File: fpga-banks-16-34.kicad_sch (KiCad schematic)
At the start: 24 parts, among them U3002 XC7K160T-FFG676, U9001 Oscillator_SMD_100MHz_ASFLMB, U9002 PCA9517A_TSSOP

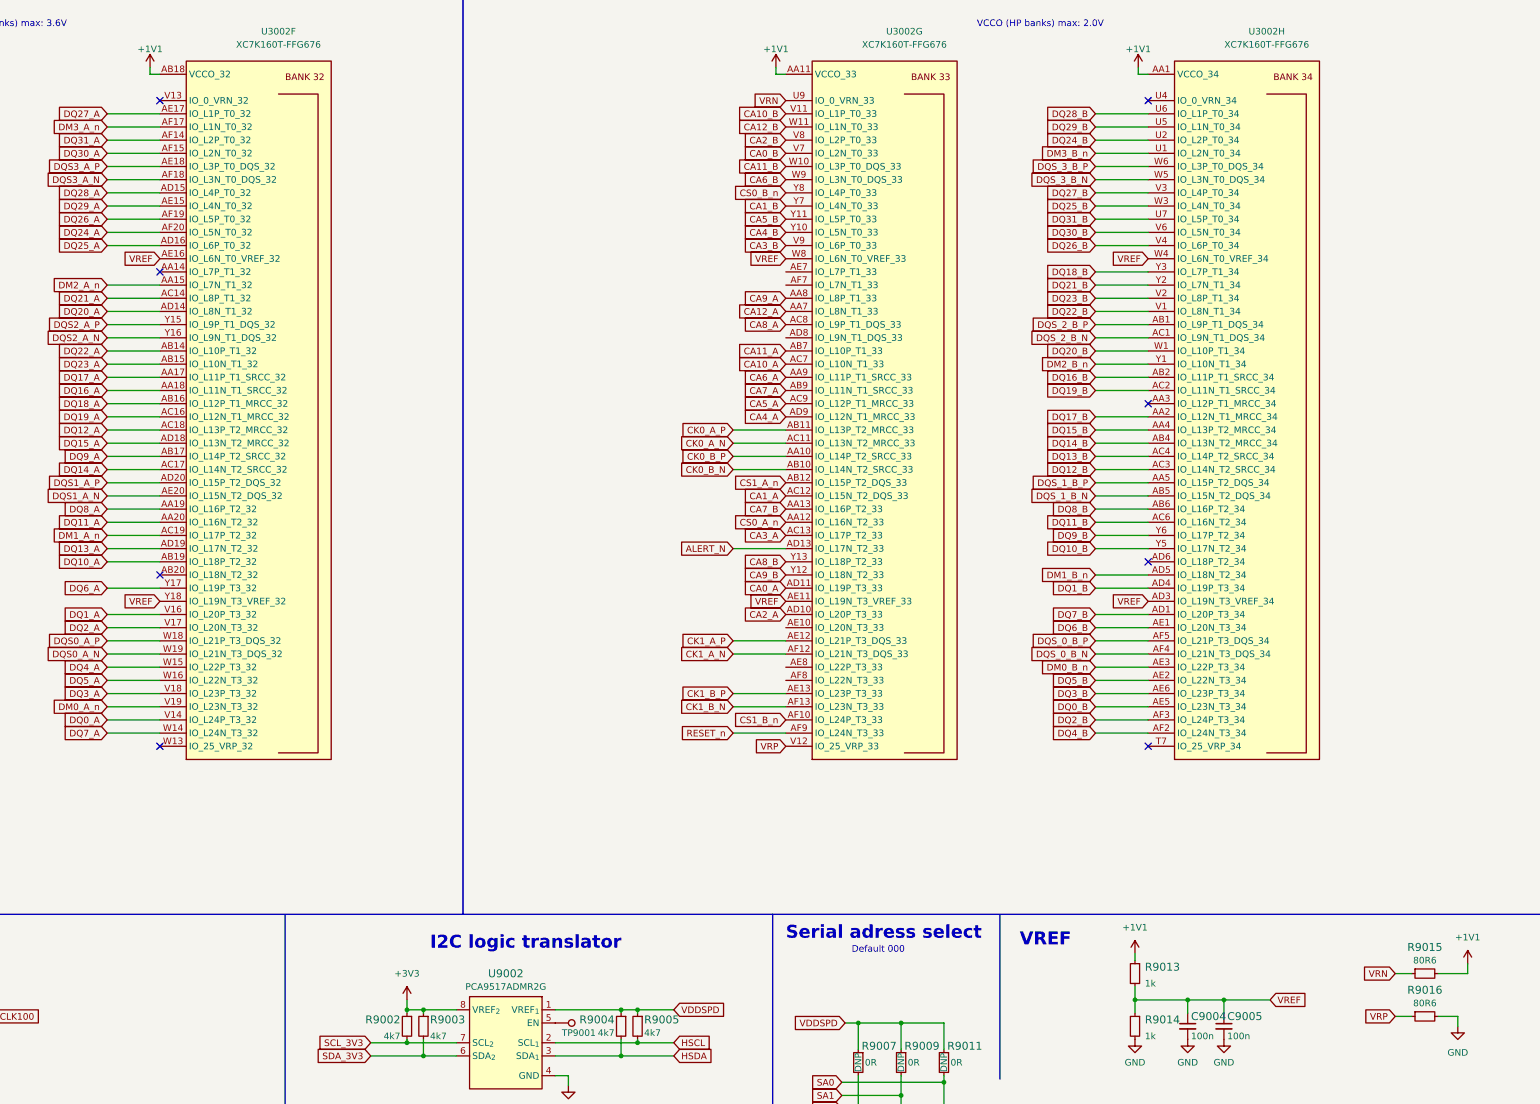
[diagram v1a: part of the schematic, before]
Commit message: Improve DDR assigment, connect ECC to remaining pins, cleanup not used components, continue placement of misc. components
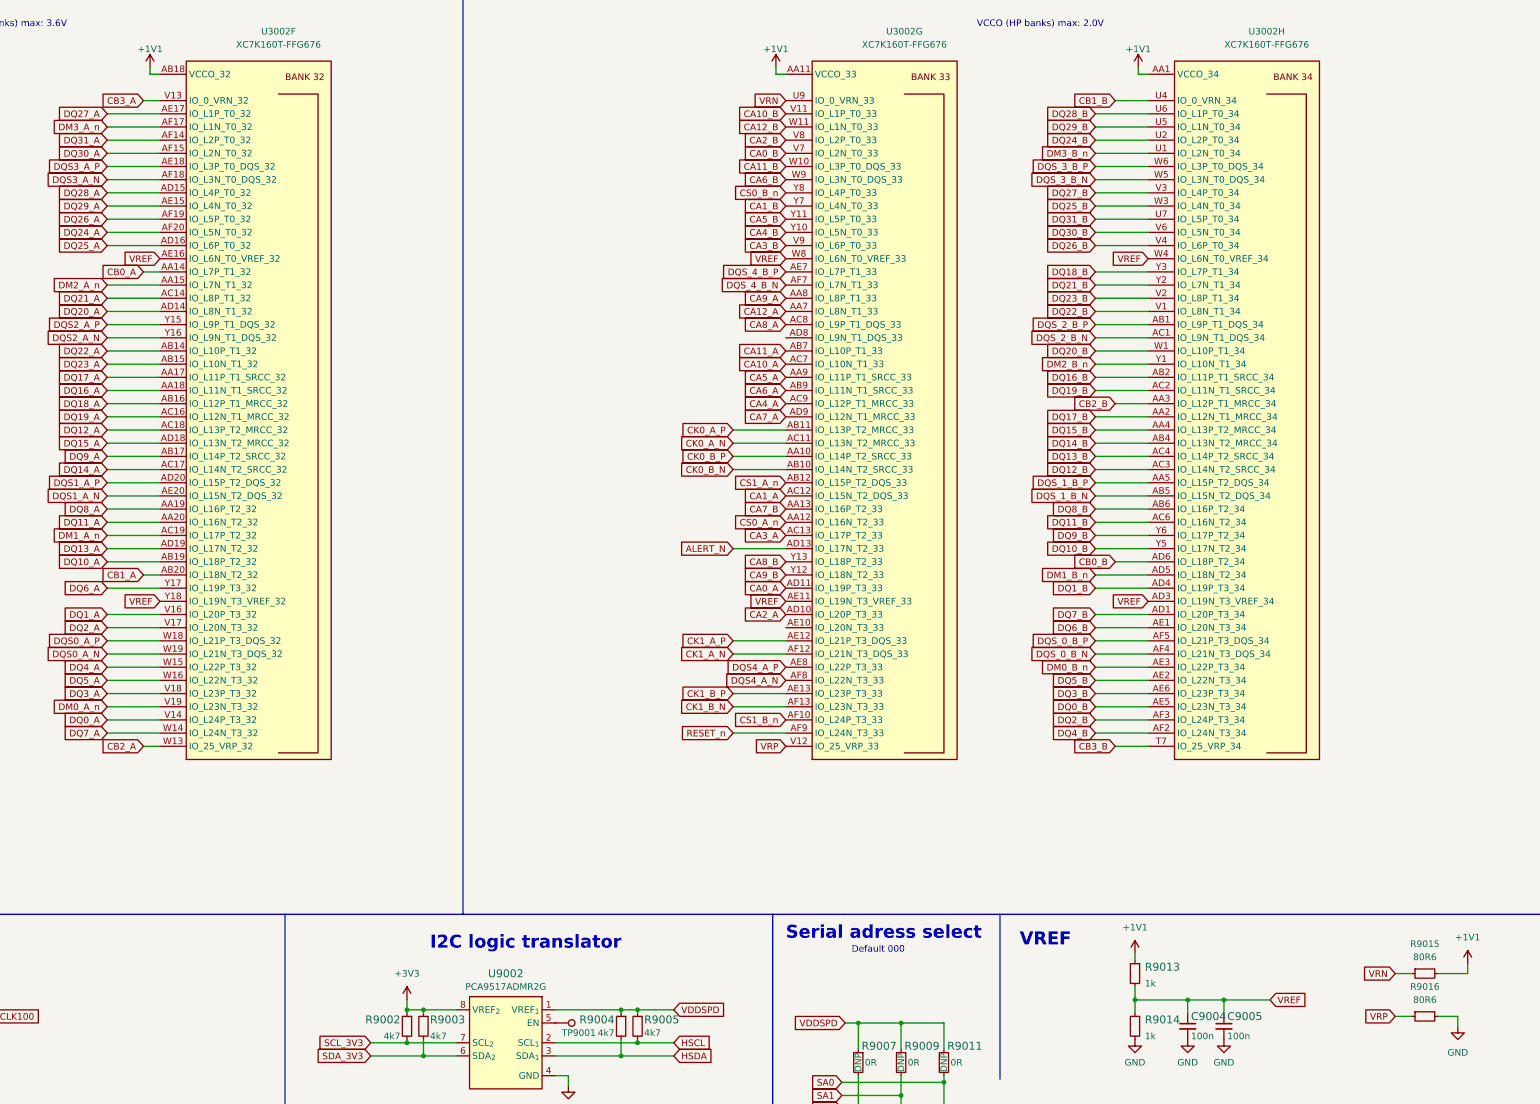
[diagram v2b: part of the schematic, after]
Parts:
- removed R9015, R9016: R_80R6_0603, data-center-rdimm-ddr4-tester-footprints:R_0603_1608Metric, symbol data-center-rdimm-ddr4-tester:R_80R6_0603
- added R9015, R9016: R_80R6_0402_EIA, antmicro-footprints:R_0402_1005Metric_EIA, symbol Resistors0402:R_80R6_0402_EIA
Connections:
- net +1V1: now also R9015.2
- net CA4_A: now also U3002.AC9 (IO_L12P_T1_MRCC_33); no longer U3002.AD9 (IO_L12N_T1_MRCC_33)
- net CA5_A: now also U3002.AA9 (IO_L11P_T1_SRCC_33); no longer U3002.AC9 (IO_L12P_T1_MRCC_33)
- net CA6_A: now also U3002.AB9 (IO_L11N_T1_SRCC_33); no longer U3002.AA9 (IO_L11P_T1_SRCC_33)
- net CA7_A: now also U3002.AD9 (IO_L12N_T1_MRCC_33); no longer U3002.AB9 (IO_L11N_T1_SRCC_33)
- net GND: now also R9016.2
- net VRN: now also R9015.1
- net VRP: now also R9016.1
- net CB0_A: now reaches U3002.AA14 (IO_L7P_T1_32)
- net CB1_A: now reaches U3002.AB20 (IO_L18N_T2_32)
- net CB3_A: now reaches U3002.V13 (IO_0_VRN_32)
- net CB2_A: now reaches U3002.W13 (IO_25_VRP_32)
- net DQS_4_B_P: now reaches U3002.AE7 (IO_L7P_T1_33)
- net DQS4_A_P: now reaches U3002.AE8 (IO_L22P_T3_33)
- net DQS_4_B_N: now reaches U3002.AF7 (IO_L7N_T1_33)
- net DQS4_A_N: now reaches U3002.AF8 (IO_L22N_T3_33)
- net CB2_B: now reaches U3002.AA3 (IO_L12P_T1_MRCC_34)
- net CB0_B: now reaches U3002.AD6 (IO_L18P_T2_34)
- net CB3_B: now reaches U3002.T7 (IO_25_VRP_34)
- net CB1_B: now reaches U3002.U4 (IO_0_VRN_34)
- no-connect marks 41 -> 33

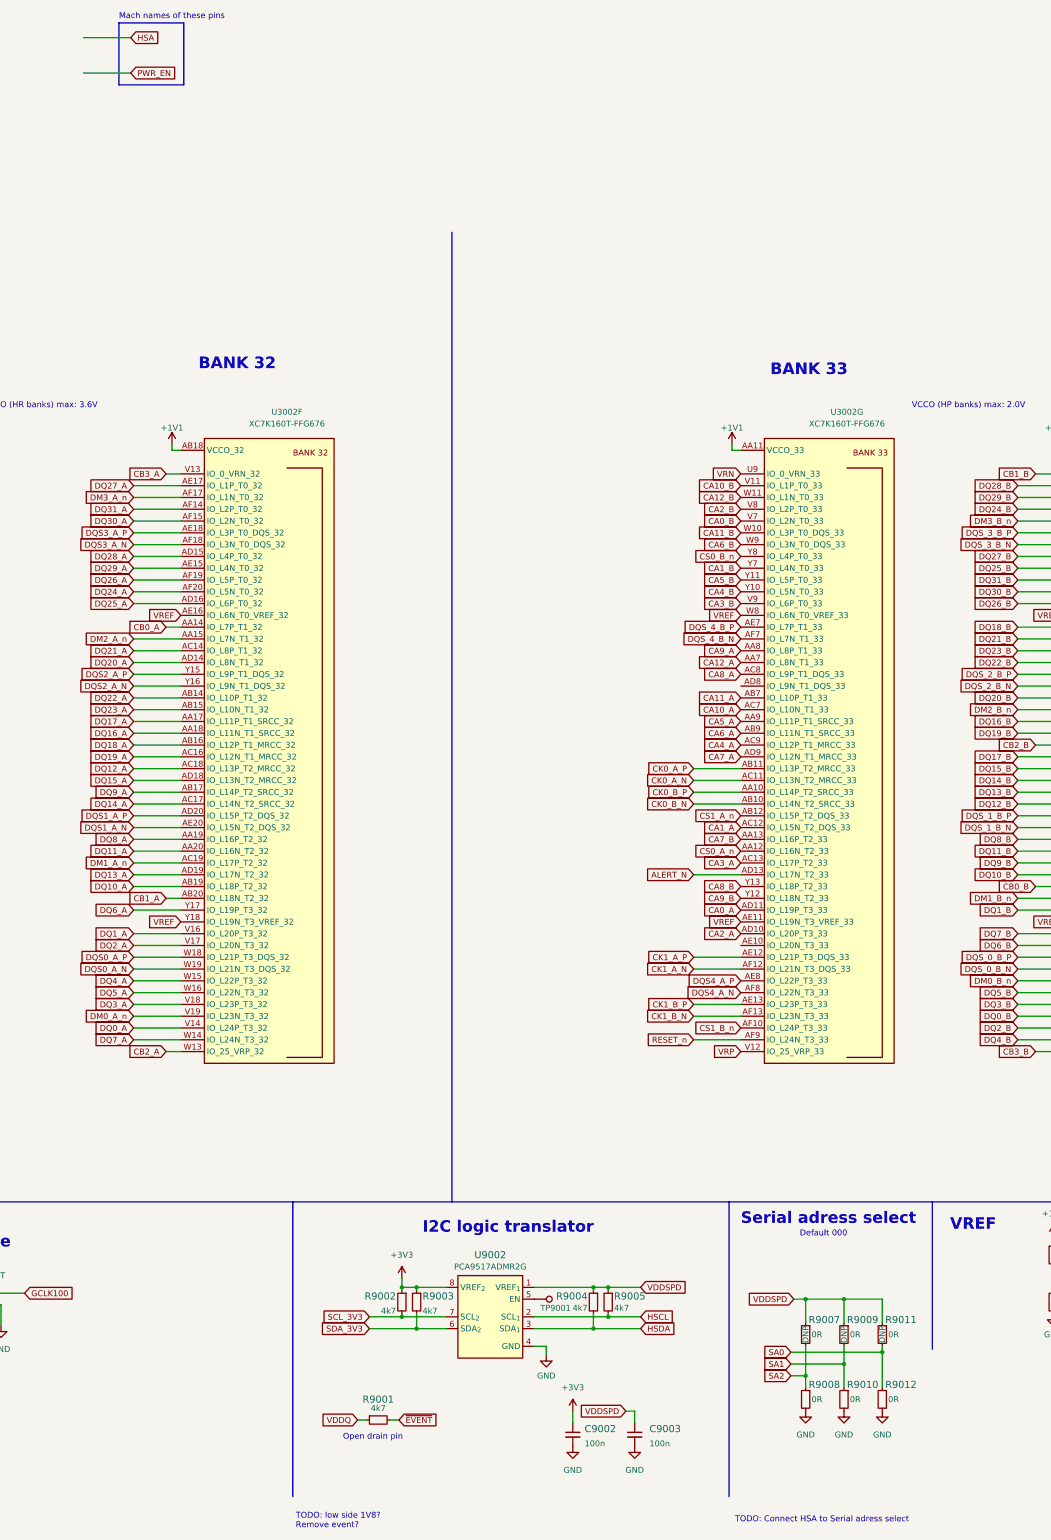
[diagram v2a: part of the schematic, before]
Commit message: Schematic cleanup, connect VINT DC-DC, continue placing misc. circuits
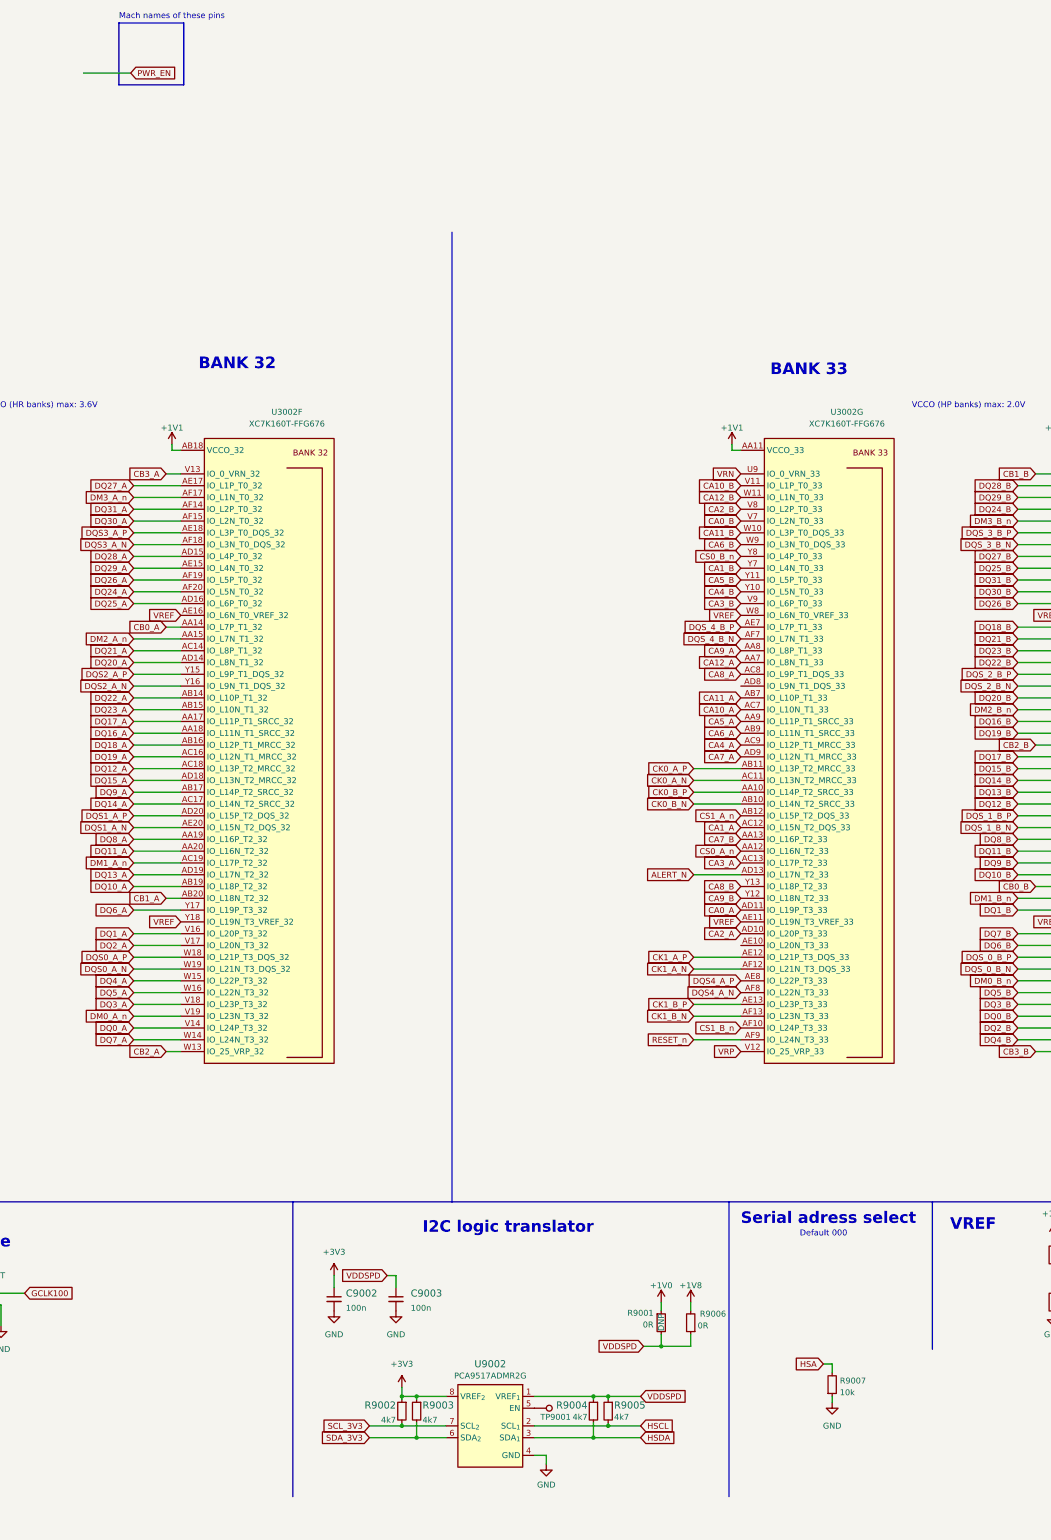
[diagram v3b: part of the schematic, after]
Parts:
- removed R9001: R_4k7_0402, data-center-rdimm-ddr4-tester-footprints:R_0402_1005Metric, symbol data-center-rdimm-ddr4-tester:R_4k7_0402
- removed R9007, R9008, R9009, R9010, R9011, R9012: R_0R_0402, data-center-rdimm-ddr4-tester-footprints:R_0402_1005Metric, symbol data-center-rdimm-ddr4-tester:R_0R_0402
- added R9001, R9006: R_0R_0402, antmicro-footprints:R_0402_1005Metric, symbol antmicroResistors0402:R_0R_0402
- added R9007: R_10k_0402, antmicro-footprints:R_0402_1005Metric, symbol antmicroResistors0402:R_10k_0402
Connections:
- net GND: now also R9007.1
- net HSA: now also R9007.2
- net VDDSPD: now also R9001.2, R9006.1
- new net +1V0: R9001.1
- new net +1V8: R9006.2
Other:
- note removed: "Open drain pin"
- note removed: "TODO: Connect HSA to Serial adress select"
- note removed: "TODO: low side 1V8? Remove event?"
- moved on the sheet: C9002, C9003, R9002, R9003, R9004, R9005, TP9001, U9002

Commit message: Add loclib
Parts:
- C9001, C9002, C9003, C9004, C9005: footprint data-center-rdimm-ddr4-tester-footprints:C_0402_1005Metric -> sodimm-ddr5-tester-footprints:C_0402_1005Metric; symbol data-center-rdimm-ddr4-tester:C_100n_0402 -> sodimm-ddr5-tester:C_100n_0402
- R9001, R9006: footprint antmicro-footprints:R_0402_1005Metric -> sodimm-ddr5-tester-footprints:R_0402_1005Metric; symbol antmicroResistors0402:R_0R_0402 -> sodimm-ddr5-tester:R_0R_0402
- R9002, R9003, R9004, R9005: footprint data-center-rdimm-ddr4-tester-footprints:R_0402_1005Metric -> sodimm-ddr5-tester-footprints:R_0402_1005Metric; symbol data-center-rdimm-ddr4-tester:R_4k7_0402 -> sodimm-ddr5-tester:R_4k7_0402
- R9007: footprint antmicro-footprints:R_0402_1005Metric -> sodimm-ddr5-tester-footprints:R_0402_1005Metric; symbol antmicroResistors0402:R_10k_0402 -> sodimm-ddr5-tester:R_10k_0402
- R9013, R9014: footprint data-center-rdimm-ddr4-tester-footprints:R_0603_1608Metric -> sodimm-ddr5-tester-footprints:R_0603_1608Metric; symbol data-center-rdimm-ddr4-tester:R_1k_0603 -> sodimm-ddr5-tester:R_1k_0603
- R9015, R9016: footprint antmicro-footprints:R_0402_1005Metric_EIA -> sodimm-ddr5-tester-footprints:R_0402_1005Metric_EIA; symbol Resistors0402:R_80R6_0402_EIA -> sodimm-ddr5-tester:R_80R6_0402_EIA
- TP9001: footprint data-center-rdimm-ddr4-tester-footprints:Testpoint_smd_1mm -> sodimm-ddr5-tester-footprints:Testpoint_smd_1mm; symbol data-center-rdimm-ddr4-tester:TP_1mm_SMD -> sodimm-ddr5-tester:TP_1mm_SMD
- U3002: footprint data-center-rdimm-ddr4-tester-footprints:BGA-676_27x27mm_Layout26x26_P1X1mm -> sodimm-ddr5-tester-footprints:BGA-676_27x27mm_Layout26x26_P1X1mm; symbol data-center-rdimm-ddr4-tester:XC7K160T-FFG676 -> sodimm-ddr5-tester:XC7K160T-FFG676
- U9001: footprint data-center-rdimm-ddr4-tester-footprints:Oscillator_SMD_Abracon_ASFLMB_5x3.2x0.85mm -> sodimm-ddr5-tester-footprints:Oscillator_SMD_Abracon_ASFLMB_5x3.2x0.85mm; symbol data-center-rdimm-ddr4-tester:Oscillator_SMD_100MHz_ASFLMB -> sodimm-ddr5-tester:Oscillator_SMD_100MHz_ASFLMB
- U9002: footprint data-center-rdimm-ddr4-tester-footprints:TSSOP-8_3x3mm_P0.65mm -> sodimm-ddr5-tester-footprints:TSSOP-8_3x3mm_P0.65mm; symbol data-center-rdimm-ddr4-tester:PCA9517A_TSSOP -> sodimm-ddr5-tester:PCA9517A_TSSOP

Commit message: Bump revision to 1.0.0
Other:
- title: LPDDR5 Test Board -> SO-DIMM DDR5 Tester
